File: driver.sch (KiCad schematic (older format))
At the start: 29 parts, among them Q1 Q_NMOS_DGS, Q2 Q_NMOS_DGS, Q3 Q_NMOS_DGS, Q4 Q_NMOS_DGS, Q5 Q_NMOS_DGS, Q6 Q_NMOS_DGS, U2 DRV8313

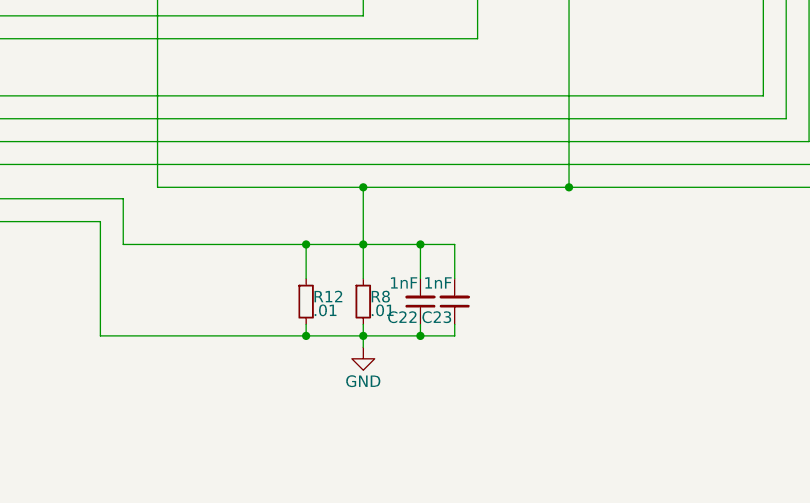
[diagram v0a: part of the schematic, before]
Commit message: changed that capacitor to a more reasonable value
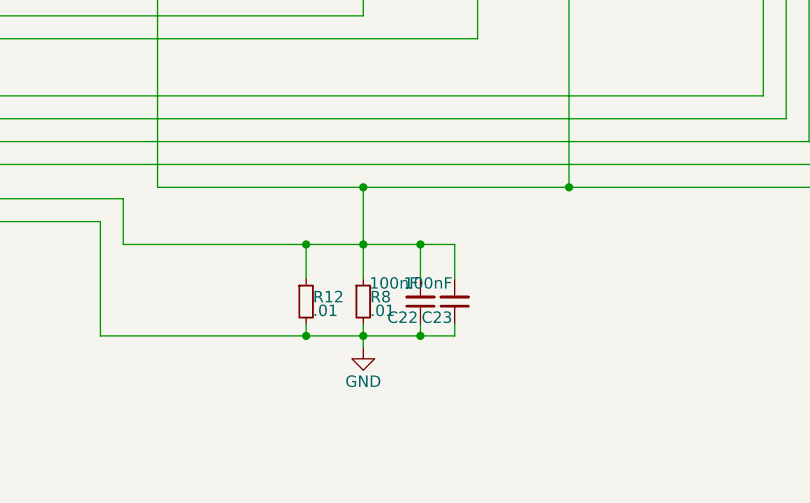
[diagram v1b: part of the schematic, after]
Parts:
- C22, C23: value 1nF -> 100nF
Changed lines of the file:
@@
 P 6000 5550
 F 0 "C22" H 6010 5620 50  0000 L CNN
-F 1 "1nF" H 6010 5470 50  0000 L CNN
+F 1 "100nF" H 6010 5470 50  0000 L CNN
 F 2 "Capacitors_SMD:C_0603" H 6000 5550 50  0001 C CNN
 F 3 "" H 6000 5550 50  0000 C CNN
@@
 P 6150 5550
 F 0 "C23" H 6160 5620 50  0000 L CNN
-F 1 "1nF" H 6160 5470 50  0000 L CNN
+F 1 "100nF" H 6160 5470 50  0000 L CNN
 F 2 "Capacitors_SMD:C_0603" H 6150 5550 50  0001 C CNN
 F 3 "" H 6150 5550 50  0000 C CNN

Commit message: long forgotten commit of something I did half a year ago -.-
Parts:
- C11, C15, C16, C17, C18, C19, C2, C21, C22, C23: footprint Capacitors_SMD:C_0603 -> Capacitor_SMD:C_0603_1608Metric; symbol C_Small -> bldc-controller-rescue:C_Small
- C20: footprint Capacitors_ThroughHole:C_Radial_D5_L11_P2 -> Capacitor_SMD:CP_Elec_5x3; symbol CP1_Small -> bldc-controller-rescue:CP1_Small
- Q1, Q2, Q3, Q4, Q5, Q6: symbol Q_NMOS_DGS -> bldc-controller-rescue:Q_NMOS_DGS
- R10, R11, R13, R14, R2, R4, R6, R7, R9: footprint Resistors_SMD:R_0603 -> Resistor_SMD:R_0603_1608Metric; symbol R_Small -> bldc-controller-rescue:R_Small
- R12, R8: footprint Resistors_SMD:R_1210 -> Resistor_SMD:R_1206_3216Metric; symbol R_Small -> bldc-controller-rescue:R_Small
- U2: symbol DRV8313 -> bldc-controller-rescue:DRV8313
